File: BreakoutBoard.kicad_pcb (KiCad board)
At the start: 4 copper layers, 74 x 55 mm, 57 parts, among them J1 PJ-063AH, J10 10129381-906001BLF, J2 10129381-906001BLF, J3 10129381-906001BLF, J4 10129381-906001BLF, J5 RJHSE-5381, J6 10129381-906001BLF, J9 10129381-914001BLF, SW1 TS02-66-43, SW2 TS02-66-43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

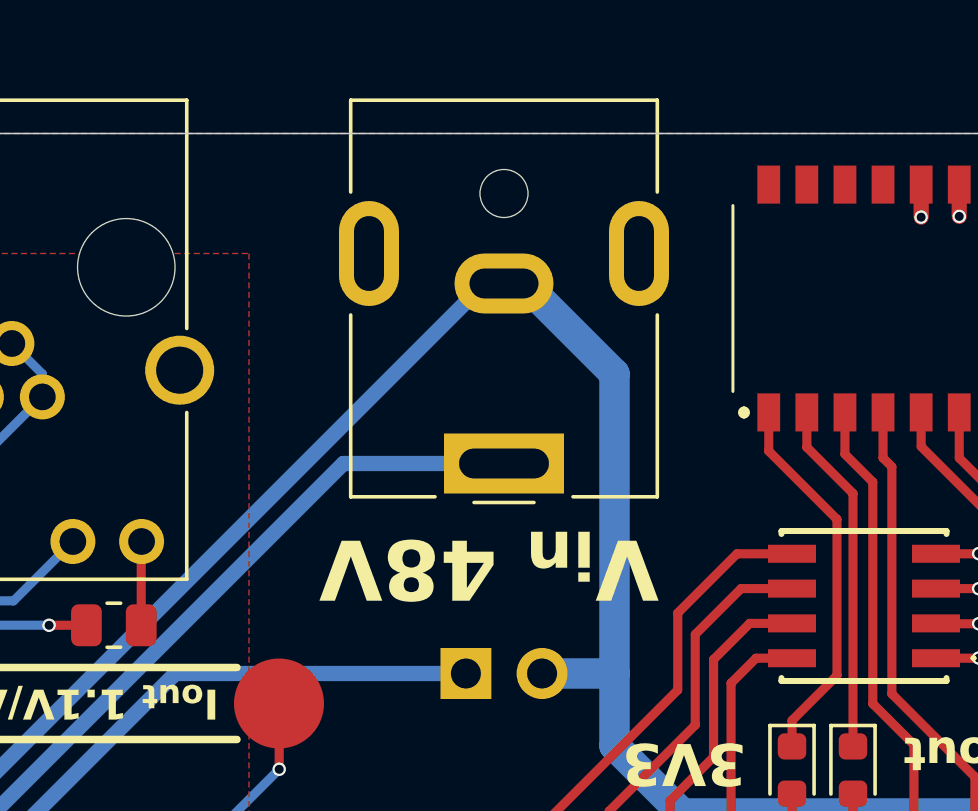
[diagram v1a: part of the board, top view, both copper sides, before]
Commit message: added external adapter voltage and polarity clarification on silk screen
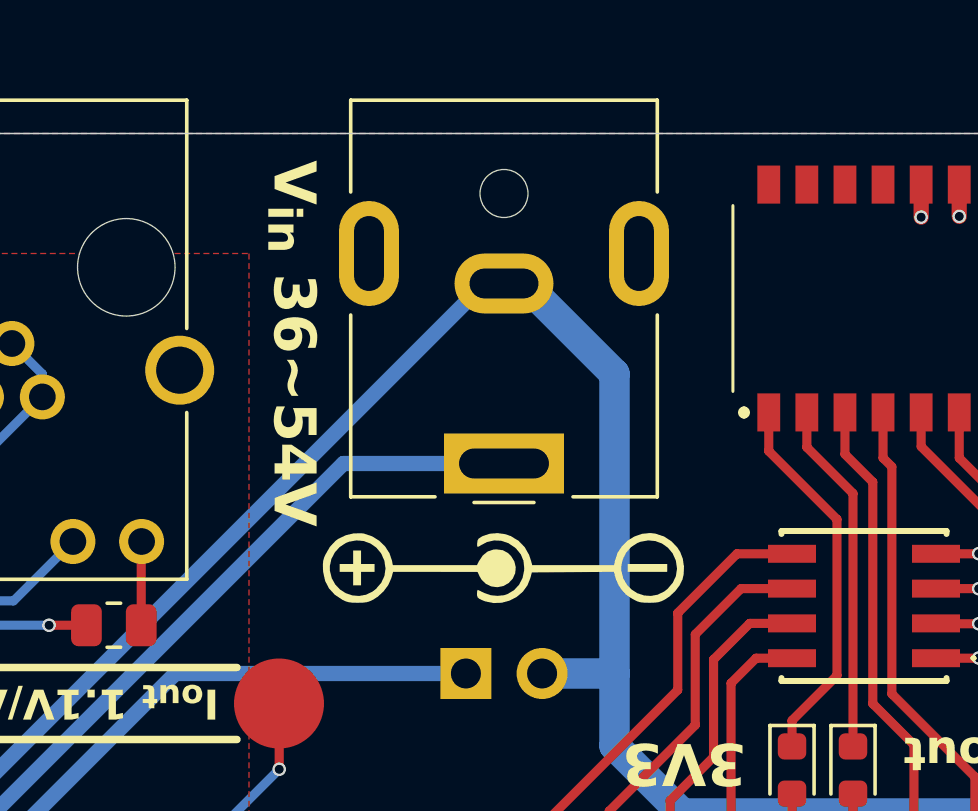
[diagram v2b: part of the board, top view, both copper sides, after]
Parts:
- added G***: LOGO, LOGO, F.Cu at (124.5, 105.5)
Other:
- board text added: "V_{in} 36~54V"
- board text removed: "V_{in} 48V"
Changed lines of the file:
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@@
 		)
 	)
+	(footprint "LOGO"
+		(layer "F.Cu")
+		(at 124.5 105.5 180)
+		(property "Reference" "G***"
+			(at 0 0 0)
+			(layer "F.SilkS")
+			(hide yes)
+			(effects
+				(font
+					(size 1.5 1.5)
+					(thickness 0.3)
+				)
+			)
+		)
+		(property "Value" "LOGO"
+			(at 0.75 0 0)
+			(layer "F.SilkS")
+			(hide yes)
+			(effects
+				(font
+					(size 1.5 1.5)
+					(thickness 0.3)
+				)
+			)
+		)
+		(property "Datasheet" ""
+			(at 0 0 0)
+			(layer "F.Fab")
+			(hide yes)
+			(effects
+				(font
+					(size 1.27 1.27)
+					(thickness 0.15)
+				)
+			)
+		)
+		(property "Description" ""
+			(at 0 0 0)
+			(layer "F.Fab")
+			(hide yes)
+			(effects
+				(font
+					(size 1.27 1.27)
+					(thickness 0.15)
+				)
+			)
+		)
+		(attr board_only exclude_from_pos_files exclude_from_bom)
+		(fp_poly
+			(pts
+				(xy -4.127031 0.018758) (xy -4.127031 0.150073) (xy -4.783604 0.150073) (xy -5.440178 0.150073)
+				(xy -5.440178 0.018758) (xy -5.440178 -0.112556) (xy -4.783604 -0.112556) (xy -4.127031 -0.112556)
+			)
+			(stroke
+				(width 0)
+				(type solid)
+			)
+			(fill yes)
+			(layer "F.SilkS")
+		)
+		(fp_poly
+			(pts
+				(xy 5.027474 -0.337667) (xy 5.027474 -0.112556) (xy 5.252585 -0.112556) (xy 5.477695 -0.112556)
+				(xy 5.477695 0.018758) (xy 5.477695 0.150073) (xy 5.252585 0.150073) (xy 5.027474 0.150073) (xy 5.027474 0.375184)
+				(xy 5.027474 0.600294) (xy 4.896159 0.600294) (xy 4.764845 0.600294) (xy 4.764845 0.375184) (xy 4.764845 0.150073)
+				(xy 4.539734 0.150073) (xy 4.314623 0.150073) (xy 4.314623 0.018758) (xy 4.314623 -0.112556) (xy 4.539734 -0.112556)
+				(xy 4.764845 -0.112556) (xy 4.764845 -0.337667) (xy 4.764845 -0.562778) (xy 4.896159 -0.562778)
+				(xy 5.027474 -0.562778)
+			)
+			(stroke
+				(width 0)
+				(type solid)
+			)
+			(fill yes)
+			(layer "F.SilkS")
+		)
+		(fp_poly
+			(pts
+				(xy 5.049465 -1.139639) (xy 5.173633 -1.125266) (xy 5.276844 -1.09488) (xy 5.383899 -1.044349) (xy 5.640747 -0.873321)
+				(xy 5.832846 -0.664564) (xy 5.961171 -0.416563) (xy 6.026694 -0.1278) (xy 6.034368 -0.030569) (xy 6.037904 0.135127)
+				(xy 6.026233 0.257676) (xy 5.994378 0.368271) (xy 5.956535 0.457171) (xy 5.801618 0.723333) (xy 5.611801 0.924776)
+				(xy 5.518324 0.991965) (xy 5.274294 1.108166) (xy 5.008452 1.170722) (xy 4.745933 1.174649) (xy 4.662314 1.161825)
+				(xy 4.397718 1.073683) (xy 4.160981 0.927922) (xy 3.963589 0.735759) (xy 3.817028 0.508415) (xy 3.732786 0.257107)
+				(xy 3.732062 0.253249) (xy 3.705977 0.112554) (xy 2.304173 0.112554) (xy 0.90237 0.112554) (xy 0.84074 0.234489)
+				(xy 0.709242 0.433705) (xy 0.549153 0.56456) (xy 0.357 0.629403) (xy 0.24387 0.637813) (xy 0.038378 0.608753)
+				(xy -0.132287 0.516984) (xy -0.238415 0.412344) (xy -0.348731 0.229454) (xy -0.392252 0.034505)
+				(xy -0.38843 -0.003017) (xy 3.950015 -0.003017) (xy 3.987171 0.256085) (xy 3.990109 0.26631) (xy 4.094891 0.501925)
+				(xy 4.251337 0.692042) (xy 4.447869 0.831411) (xy 4.672914 0.914783) (xy 4.914897 0.936906) (xy 5.162241 0.892532)
+				(xy 5.274003 0.848638) (xy 5.47958 0.714631) (xy 5.642688 0.531389) (xy 5.754506 0.314344) (xy 5.806212 0.078931)
+				(xy 5.803319 -0.077378) (xy 5.741006 -0.324496) (xy 5.623941 -0.534344) (xy 5.46302 -0.702623) (xy 5.269138 -0.82503)
+				(xy 5.053192 -0.897268) (xy 4.826076 -0.915034) (xy 4.598687 -0.874029) (xy 4.381921 -0.769953)
+				(xy 4.269484 -0.682744) (xy 4.092904 -0.478318) (xy 3.985837 -0.24978) (xy 3.950015 -0.003017) (xy -0.38843 -0.003017)
+				(xy -0.372582 -0.158588) (xy -0.293322 -0.335908) (xy -0.158075 -0.483541) (xy 0.01948 -0.583807)
+				(xy 0.222229 -0.624273) (xy 0.422138 -0.598235) (xy 0.602914 -0.51223) (xy 0.748266 -0.372796) (xy 0.81188 -0.26581)
+				(xy 0.881684 -0.114492) (xy 2.288626 -0.113576) (xy 3.695568 -0.11266) (xy 3.760159 -0.332475) (xy 3.858585 -0.552436)
+				(xy 4.014148 -0.762443) (xy 4.209642 -0.942356) (xy 4.366864 -1.042687) (xy 4.477343 -1.094702)
+				(xy 4.580954 -1.125231) (xy 4.704887 -1.139632) (xy 4.876332 -1.143261) (xy 4.8774 -1.143261)
+			)
+			(stroke
+				(width 0)
+				(type solid)
+			)
+			(fill yes)
+			(layer "F.SilkS")
+		)
+		(fp_poly
+			(pts
+				(xy 0.612432 -1.099997) (xy 0.726485 -1.05665) (xy 0.830361 -1.00579) (xy 0.881874 -0.959042) (xy 0.899071 -0.894582)
+				(xy 0.900443 -0.846276) (xy 0.895485 -0.758598) (xy 0.883273 -0.714199) (xy 0.880436 -0.712852)
+				(xy 0.838833 -0.728621) (xy 0.751666 -0.769459) (xy 0.664705 -0.812882) (xy 0.452842 -0.887218)
+				(xy 0.220209 -0.913208) (xy -0.003934 -0.889288) (xy -0.112556 -0.854474) (xy -0.332122 -0.723513)
+				(xy -0.50282 -0.540804) (xy -0.618062 -0.316589) (xy -0.671262 -0.061109) (xy -0.674142 0.018758)
+				(xy -0.646679 0.263875) (xy -0.5605 0.471479) (xy -0.408282 0.657619) (xy -0.364029 0.698319) (xy -0.147942 0.843551)
+				(xy 0.088027 0.923129) (xy 0.331219 0.936106) (xy 0.568973 0.881534) (xy 0.756161 0.782148) (xy 0.844202 0.727085)
+				(xy 0.887002 0.726261) (xy 0.897334 0.786326) (xy 0.893328 0.853544) (xy 0.879313 0.93968) (xy 0.842728 0.998092)
+				(xy 0.765123 1.050719) (xy 0.698755 1.084908) (xy 0.470877 1.159792) (xy 0.216262 1.179969) (xy -0.040587 1.145546)
+				(xy -0.22684 1.080805) (xy -0.485077 0.922948) (xy -0.688028 0.714411) (xy -0.835253 0.455727) (xy -0.897975 0.271797)
+				(xy -0.940854 0.112554) (xy -2.304657 0.112554) (xy -3.668459 0.112554) (xy -3.694526 0.251504)
+				(xy -3.779048 0.509108) (xy -3.923484 0.736088) (xy -4.116283 0.924692) (xy -4.345892 1.067172)
+				(xy -4.600761 1.155776) (xy -4.869338 1.182755) (xy -5.052096 1.162316) (xy -5.331654 1.068557)
+				(xy -5.578098 0.911555) (xy -5.779997 0.699748) (xy -5.870346 0.5585) (xy -5.959837 0.325661) (xy -5.999902 0.062867)
+				(xy -5.996968 -0.003017) (xy -5.767267 -0.003017) (xy -5.730111 0.256085) (xy -5.727174 0.26631)
+				(xy -5.622391 0.501925) (xy -5.465946 0.692042) (xy -5.269413 0.831411) (xy -5.044368 0.914783)
+				(xy -4.802386 0.936906) (xy -4.555041 0.892532) (xy -4.44328 0.848638) (xy -4.237703 0.714631) (xy -4.074594 0.531389)
+				(xy -3.962776 0.314344) (xy -3.91107 0.078931) (xy -3.913963 -0.077378) (xy -3.976276 -0.324496)
+				(xy -4.093341 -0.534344) (xy -4.254262 -0.702623) (xy -4.448144 -0.82503) (xy -4.66409 -0.897268)
+				(xy -4.891206 -0.915034) (xy -5.118595 -0.874029) (xy -5.335361 -0.769953) (xy -5.447799 -0.682744)
+				(xy -5.624378 -0.478318) (xy -5.731446 -0.24978) (xy -5.767267 -0.003017) (xy -5.996968 -0.003017)
+				(xy -5.988135 -0.201355) (xy -5.948656 -0.369228) (xy -5.854704 -0.561221) (xy -5.708544 -0.75321)
+				(xy -5.529712 -0.923202) (xy -5.350418 -1.042687) (xy -5.23994 -1.094702) (xy -5.136328 -1.125231)
+				(xy -5.012395 -1.139632) (xy -4.84095 -1.143261) (xy -4.839882 -1.143261) (xy -4.66982 -1.139874)
+				(xy -4.547944 -1.126138) (xy -4.447569 -1.096693) (xy -4.342011 -1.04618) (xy -4.333383 -1.041524)
+				(xy -4.213381 -0.972008) (xy -4.110065 -0.904616) (xy -4.067841 -0.87244) (xy -3.933065 -0.725537)
+				(xy -3.811941 -0.540123) (xy -3.725943 -0.35067) (xy -3.710252 -0.298389) (xy -3.662391 -0.111647)
+				(xy -2.294939 -0.121481) (xy -0.927488 -0.131316) (xy -0.881507 -0.312442) (xy -0.781452 -0.563555)
+				(xy -0.624912 -0.777119) (xy -0.423106 -0.947943) (xy -0.18725 -1.070834) (xy 0.071436 -1.140601)
+				(xy 0.341736 -1.152053)
+			)
+			(stroke
+				(width 0)
+				(type solid)
+			)
+			(fill yes)
+			(layer "F.SilkS")
+		)
+		(embedded_fonts no)
+	)
 	(footprint "Capacitor_SMD:C_0805_2012Metric"
 		(layer "F.Cu")
@@
 		)
 	)
-	(gr_text "V_{in} 48V"
-		(at 124 105.5 180)
+	(gr_text "V_{in} 36~54V"
+		(at 117.5 98 270)
 		(layer "F.SilkS")
 		(effects
 			(font
-				(size 2 2)
-				(thickness 0.4)
+				(size 1.4 1.4)
+				(thickness 0.28)
 				(bold yes)
 			)
